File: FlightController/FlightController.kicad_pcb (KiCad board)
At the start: 6 copper layers, 45 x 44 mm, 30 parts, among them J1 FTSH-107-01-L-DV-K-A, J3 M55-7104042R, J5 Conn_01x02_Pin, SW1 SW_TL1015AF160QG, SW2 SW_TL1015AF160QG, U1 STM32L496RGT6TR, U5 BNO086, U9 TCAN332DCNR, Y2 XTAL_ABS07-32.768KHZ-T

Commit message: Updates to FC
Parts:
- removed J1: FTSH-107-01-L-DV-K-A, inspirefly:SAMTEC_FTSH-107-01-L-DV-K-A
- added C8: 100nF, Capacitor_SMD:C_0402_1005Metric_Pad0.74x0.62mm_HandSolder, F.Cu at (154.9, 78.0)
- added C9: 47uF, Capacitor_SMD:C_1206_3216Metric_Pad1.33x1.80mm_HandSolder, F.Cu at (99.9, 54.6)
- added IC1: MX25L25645GM2I-08G-TR, Package_SO:SOIC-8_5.3x5.3mm_P1.27mm, F.Cu at (148.3, 82.5)
- C1, C18, C2, C22, C24, C25, C26, C27, C28, C3, C33, C4, C5, C6, C7: footprint Capacitor_SMD:C_0402_1005Metric -> Capacitor_SMD:C_0402_1005Metric_Pad0.74x0.62mm_HandSolder
- R10, R2, R22, R25, R7: footprint Resistor_SMD:R_0402_1005Metric -> Resistor_SMD:R_0402_1005Metric_Pad0.72x0.64mm_HandSolder
- moved RN1 84.0 mm to (167.8, 65.3)
- moved SW2 70.6 mm to (169.1, 50.9)
- moved SW1 69.1 mm to (170.1, 55.9)
- moved C2 64.8 mm to (154.6, 44.9)
- moved C3 64.8 mm to (154.6, 46.8)
- moved C1 62.3 mm to (153.8, 53.5)
- moved Y2 58.7 mm to (159.2, 46.5)
- moved U9 47.4 mm to (125.5, 83.4)
- moved J5 42.0 mm to (72.8, 45.7)
- moved R2 41.9 mm to (150.8, 55.9)
- moved C4 40.7 mm to (132.3, 67.6)
- moved C5 40.7 mm to (132.3, 69.5)
- moved R7 39.7 mm to (149.4, 52.5)
- moved C22 38.4 mm to (131.7, 72.2)
- moved C33 37.3 mm to (130.0, 80.6)
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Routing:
- net +3.3V: track 0.00 -> 28.6 mm, vias 0 -> 5
- added copper zone on In2.Cu, net +3.3V
- removed copper zone on In3.Cu, net +3.3V
- removed copper zone on In2.Cu, net GND
- removed copper zone on In4.Cu, net GND
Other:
- copper layers 6 -> 4

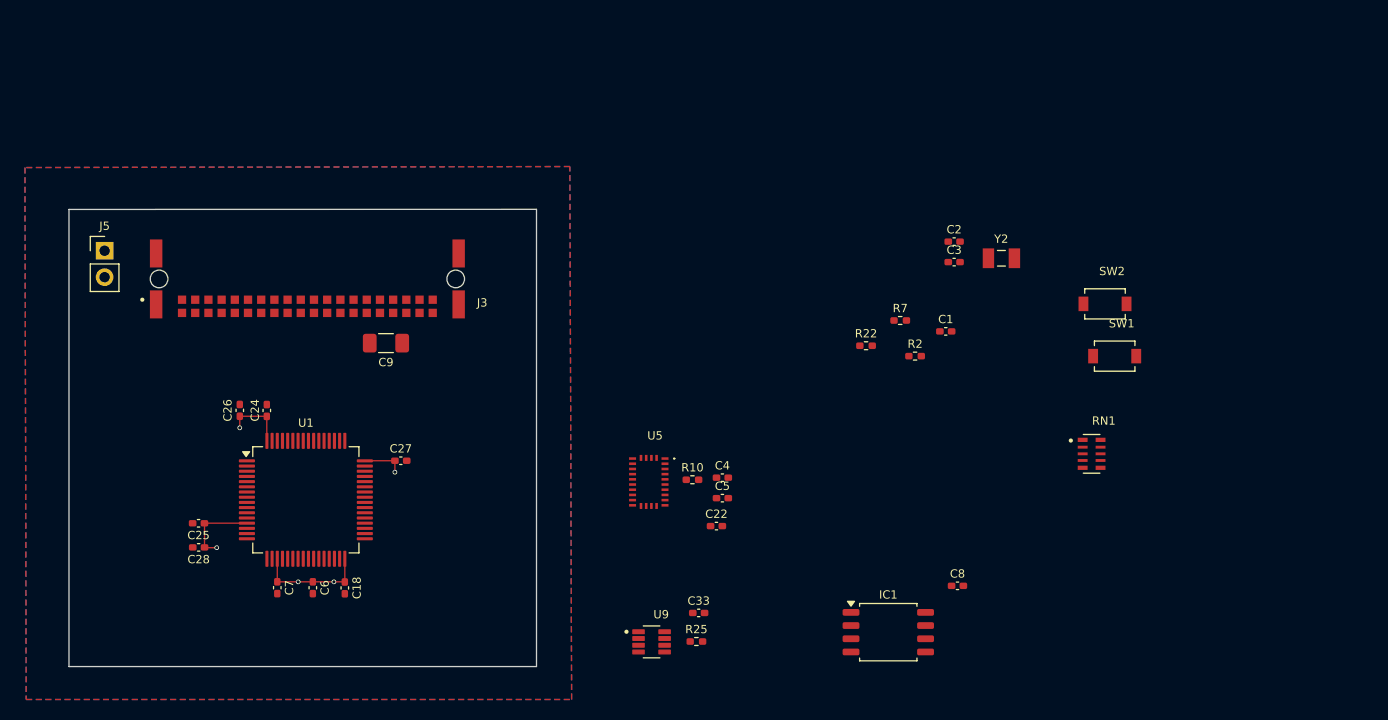
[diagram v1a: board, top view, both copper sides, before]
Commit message: Sorting files/ cleanup
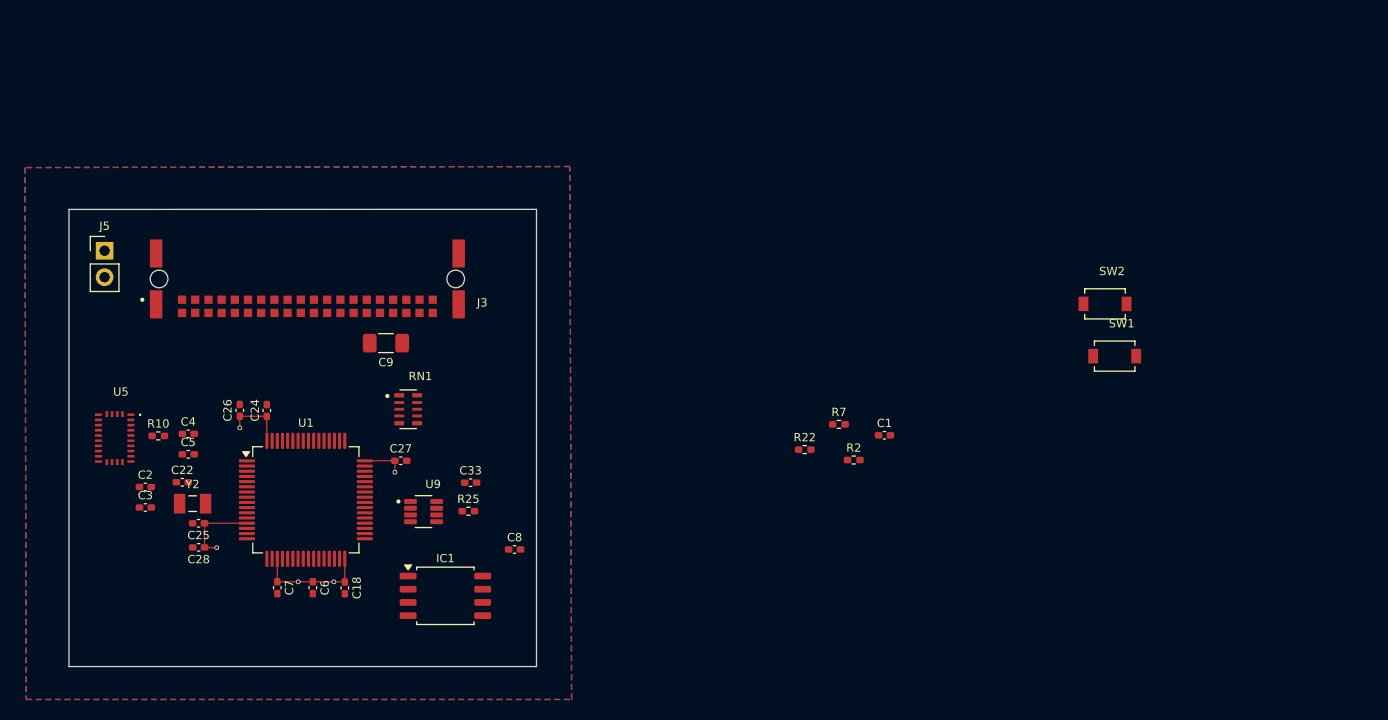
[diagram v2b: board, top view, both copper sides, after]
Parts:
- moved Y2 81.4 mm to (81.3, 70.1)
- moved C2 81.4 mm to (76.8, 68.5)
- moved C3 81.4 mm to (76.8, 70.5)
- moved RN1 65.9 mm to (102.0, 61.0)
- moved C22 51.6 mm to (80.3, 68.0)
- moved C4 51.6 mm to (80.9, 63.4)
- moved C5 51.6 mm to (80.9, 65.3)
- moved R10 51.6 mm to (78.0, 63.6)
- moved U5 51.6 mm to (73.8, 63.8)
- moved IC1 42.8 mm to (105.6, 79.0)
- moved C8 42.8 mm to (112.3, 74.5)
- moved U9 25.3 mm to (103.5, 70.8)
- moved C33 25.3 mm to (108.1, 68.1)
- moved R25 25.3 mm to (107.8, 70.8)
- moved R7 11.6 mm to (143.5, 62.5)
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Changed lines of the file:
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@@
 	(footprint "Capacitor_SMD:C_0402_1005Metric_Pad0.74x0.62mm_HandSolder"
 		(layer "F.Cu")
-		(at 153.7925 53.5)
+		(at 147.8925 63.5)
 		(descr "Capacitor SMD 0402 (1005 Metric), square (rectangular) end terminal, IPC-7351 nominal with elongated pad for handsoldering. (Body size source: IPC-SM-782 page 76, https://www.pcb-3d.com/wordpress/wp-content/uploads/ipc-sm-782a_amendment_1_and_2.pdf), generated with kicad-footprint-generator")
 		(tags "capacitor handsolder")
@@
 	(footprint "Package_SO:SOIC-8_5.3x5.3mm_P1.27mm"
 		(layer "F.Cu")
-		(at 148.26 82.45)
+		(at 105.63 78.9525)
 		(descr "SOIC, 8 Pin (JEITA/EIAJ ED-7311-19 variation 08-001-BBA and Atmel/Microchip, 208 mils width, https://www.jeita.or.jp/japanese/standard/book/ED-7311-19/#target/page_no=21, https://ww1.microchip.com/downloads/en/DeviceDoc/20005045C.pdf#page=23, https://ww1.microchip.com/downloads/en/DeviceDoc/doc2535.pdf#page=162), generated with kicad-footprint-generator ipc_gullwing_generator.py")
 		(tags "SOIC SO P-SOP SOP SOP-8 SO SO-8 8S2 S2AE/F K04-056 CASE-751BE SO8W 8-Pin-SOIC PSA W8-2 W8-4 W8MS-1 FPT-8P-M08")
@@
 	(footprint "Capacitor_SMD:C_0402_1005Metric_Pad0.74x0.62mm_HandSolder"
 		(layer "F.Cu")
-		(at 132.2925 69.55)
+		(at 80.88 65.33)
 		(descr "Capacitor SMD 0402 (1005 Metric), square (rectangular) end terminal, IPC-7351 nominal with elongated pad for handsoldering. (Body size source: IPC-SM-782 page 76, https://www.pcb-3d.com/wordpress/wp-content/uploads/ipc-sm-782a_amendment_1_and_2.pdf), generated with kicad-footprint-generator")
 		(tags "capacitor handsolder")
@@
 	(footprint "inspirefly:BNO086"
 		(layer "F.Cu")
-		(at 125.208 67.99)
+		(at 73.7955 63.77)
 		(descr "BNO086-1")
 		(tags "Undefined or Miscellaneous")
@@
 	(footprint "Resistor_SMD:R_0402_1005Metric_Pad0.72x0.64mm_HandSolder"
 		(layer "F.Cu")
-		(at 129.41 67.78)
+		(at 77.9975 63.56)
 		(descr "Resistor SMD 0402 (1005 Metric), square (rectangular) end terminal, IPC-7351 nominal with elongated pad for handsoldering. (Body size source: IPC-SM-782 page 72, https://www.pcb-3d.com/wordpress/wp-content/uploads/ipc-sm-782a_amendment_1_and_2.pdf), generated with kicad-footprint-generator")
 		(tags "resistor handsolder")
@@
 	(footprint "Resistor_SMD:R_0402_1005Metric_Pad0.72x0.64mm_HandSolder"
 		(layer "F.Cu")
-		(at 146.12 54.88)
+		(at 140.22 64.88)
 		(descr "Resistor SMD 0402 (1005 Metric), square (rectangular) end terminal, IPC-7351 nominal with elongated pad for handsoldering. (Body size source: IPC-SM-782 page 72, https://www.pcb-3d.com/wordpress/wp-content/uploads/ipc-sm-782a_amendment_1_and_2.pdf), generated with kicad-footprint-generator")
 		(tags "resistor handsolder")
@@
 	(footprint "Capacitor_SMD:C_0402_1005Metric_Pad0.74x0.62mm_HandSolder"
 		(layer "F.Cu")
-		(at 154.6 44.86)
+		(at 76.75 68.48)
 		(descr "Capacitor SMD 0402 (1005 Metric), square (rectangular) end terminal, IPC-7351 nominal with elongated pad for handsoldering. (Body size source: IPC-SM-782 page 76, https://www.pcb-3d.com/wordpress/wp-content/uploads/ipc-sm-782a_amendment_1_and_2.pdf), generated with kicad-footprint-generator")
 		(tags "capacitor handsolder")
@@
 	(footprint "inspirefly:XTAL_ABS07-32.768KHZ-T"
 		(layer "F.Cu")
-		(at 159.15 46.46)
+		(at 81.3 70.08)
 		(property "Reference" "Y2"
 			(at -0.018 -1.8564 0)
@@
 	(footprint "Capacitor_SMD:C_0402_1005Metric_Pad0.74x0.62mm_HandSolder"
 		(layer "F.Cu")
-		(at 131.72 72.24)
+		(at 80.3075 68.02)
 		(descr "Capacitor SMD 0402 (1005 Metric), square (rectangular) end terminal, IPC-7351 nominal with elongated pad for handsoldering. (Body size source: IPC-SM-782 page 76, https://www.pcb-3d.com/wordpress/wp-content/uploads/ipc-sm-782a_amendment_1_and_2.pdf), generated with kicad-footprint-generator")
 		(tags "capacitor handsolder")
@@
 	(footprint "Capacitor_SMD:C_0402_1005Metric_Pad0.74x0.62mm_HandSolder"
 		(layer "F.Cu")
-		(at 154.6 46.83)
+		(at 76.75 70.45)
 		(descr "Capacitor SMD 0402 (1005 Metric), square (rectangular) end terminal, IPC-7351 nominal with elongated pad for handsoldering. (Body size source: IPC-SM-782 page 76, https://www.pcb-3d.com/wordpress/wp-content/uploads/ipc-sm-782a_amendment_1_and_2.pdf), generated with kicad-footprint-generator")
 		(tags "capacitor handsolder")
@@
 	(footprint "Resistor_SMD:R_0402_1005Metric_Pad0.72x0.64mm_HandSolder"
 		(layer "F.Cu")
-		(at 149.41 52.45)
+		(at 143.51 62.45)
 		(descr "Resistor SMD 0402 (1005 Metric), square (rectangular) end terminal, IPC-7351 nominal with elongated pad for handsoldering. (Body size source: IPC-SM-782 page 72, https://www.pcb-3d.com/wordpress/wp-content/uploads/ipc-sm-782a_amendment_1_and_2.pdf), generated with kicad-footprint-generator")
 		(tags "resistor handsolder")
@@
 	(footprint "inspirefly:SOT65P280X145-8N"
 		(layer "F.Cu")
-		(at 125.475 83.385)
+		(at 103.525 70.845)
 		(property "Reference" "U9"
 			(at 0.925 -2.635 0)
@@
 	(footprint "Capacitor_SMD:C_0402_1005Metric_Pad0.74x0.62mm_HandSolder"
 		(layer "F.Cu")
-		(at 154.92 77.99)
+		(at 112.29 74.4925)
 		(descr "Capacitor SMD 0402 (1005 Metric), square (rectangular) end terminal, IPC-7351 nominal with elongated pad for handsoldering. (Body size source: IPC-SM-782 page 76, https://www.pcb-3d.com/wordpress/wp-content/uploads/ipc-sm-782a_amendment_1_and_2.pdf), generated with kicad-footprint-generator")
 		(tags "capacitor handsolder")
@@
 	(footprint "Resistor_SMD:R_0402_1005Metric_Pad0.72x0.64mm_HandSolder"
 		(layer "F.Cu")
-		(at 150.84 55.88)
+		(at 144.94 65.88)
 		(descr "Resistor SMD 0402 (1005 Metric), square (rectangular) end terminal, IPC-7351 nominal with elongated pad for handsoldering. (Body size source: IPC-SM-782 page 72, https://www.pcb-3d.com/wordpress/wp-content/uploads/ipc-sm-782a_amendment_1_and_2.pdf), generated with kicad-footprint-generator")
 		(tags "resistor handsolder")
@@
 	(footprint "Resistor_SMD:R_0402_1005Metric_Pad0.72x0.64mm_HandSolder"
 		(layer "F.Cu")
-		(at 129.79 83.35)
+		(at 107.84 70.81)
 		(descr "Resistor SMD 0402 (1005 Metric), square (rectangular) end terminal, IPC-7351 nominal with elongated pad for handsoldering. (Body size source: IPC-SM-782 page 72, https://www.pcb-3d.com/wordpress/wp-content/uploads/ipc-sm-782a_amendment_1_and_2.pdf), generated with kicad-footprint-generator")
 		(tags "resistor handsolder")
@@
 	(footprint "Capacitor_SMD:C_0402_1005Metric_Pad0.74x0.62mm_HandSolder"
 		(layer "F.Cu")
-		(at 132.2925 67.58)
+		(at 80.88 63.36)
 		(descr "Capacitor SMD 0402 (1005 Metric), square (rectangular) end terminal, IPC-7351 nominal with elongated pad for handsoldering. (Body size source: IPC-SM-782 page 76, https://www.pcb-3d.com/wordpress/wp-content/uploads/ipc-sm-782a_amendment_1_and_2.pdf), generated with kicad-footprint-generator")
 		(tags "capacitor handsolder")
@@
 	(footprint "Capacitor_SMD:C_0402_1005Metric_Pad0.74x0.62mm_HandSolder"
 		(layer "F.Cu")
-		(at 130.01 80.6)
+		(at 108.06 68.06)
 		(descr "Capacitor SMD 0402 (1005 Metric), square (rectangular) end terminal, IPC-7351 nominal with elongated pad for handsoldering. (Body size source: IPC-SM-782 page 76, https://www.pcb-3d.com/wordpress/wp-content/uploads/ipc-sm-782a_amendment_1_and_2.pdf), generated with kicad-footprint-generator")
 		(tags "capacitor handsolder")
@@
 	(footprint "inspirefly:RESCAXE64P320X160X70-10N"
 		(layer "F.Cu")
-		(at 167.83 65.285)
+		(at 102.05 60.995)
 		(property "Reference" "RN1"
 			(at 1.175 -3.175 0)

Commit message: Board sizes for FC and routing. slight Backplane changes
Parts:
- removed C25: 10nF, Capacitor_SMD:C_0402_1005Metric_Pad0.74x0.62mm_HandSolder
- added C10: 22pF, Capacitor_SMD:C_0402_1005Metric_Pad0.74x0.62mm_HandSolder, F.Cu at (106.7, 48.1)
- added C11: 22pF, Capacitor_SMD:C_0402_1005Metric_Pad0.74x0.62mm_HandSolder, F.Cu at (106.7, 45.5)
- added H5: MountingHole_Pad, inspirefly:MountingHole_2mm_custom, F.Cu at (75.6, 37.0)
- added H6: MountingHole_Pad, inspirefly:MountingHole_2mm_custom, F.Cu at (108.6, 37.0)
- added Y3: XTAL_ABS07-32.768KHZ-T, inspirefly:XTAL_ABS07-32.768KHZ-T, F.Cu at (109.2, 46.6)
- moved SW2 88.9 mm to (81.3, 36.9)
- moved SW1 82.3 mm to (90.0, 36.9)
- moved R2 69.5 mm to (76.3, 55.0)
- moved C1 69.4 mm to (79.0, 55.0), turned to 180 degrees
- moved R7 63.7 mm to (85.6, 35.9)
- moved R22 60.7 mm to (85.6, 38.3), turned to 180 degrees
- moved J5 43.5 mm to (109.8, 68.7)
- moved IC1 41.7 mm to (99.4, 37.7)
- moved C8 39.9 mm to (105.2, 35.2), turned to 90 degrees
- moved C22 35.1 mm to (105.0, 43.0), turned to 90 degrees
- moved C33 35.0 mm to (85.5, 41.3), turned to 180 degrees
- moved R25 33.2 mm to (92.8, 41.2), turned to 90 degrees
- moved U9 33.0 mm to (89.5, 41.0)
- moved U5 33.0 mm to (102.8, 48.0)
- moved RN1 31.9 mm to (75.8, 42.9)
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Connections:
- J3 pad A17: GND -> SUPER_CAP_CHARGE
- U1 pad 27: IMU_BOOTN -> unconnected-(U1A-PB1-Pad27)
- U1 pad 37: unconnected-(U1A-PC6-Pad37) -> FOOTSWITCH
- U1 pad 38: EXTERNAL_BAT_CUTOFF -> SUPER_CAP_CHARGE
- U1 pad 39: HEATER_ENABLE -> IMU_BOOTN
- U5 pad 26: GND -> Net-(U5-XOUT32/CLKSEL1)
- U5 pad 27: unconnected-(U5-XIN32-Pad27) -> Net-(U5-XIN32)
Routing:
- net I2C2_SDA: track 0.00 -> 65.3 mm, vias 0 -> 4
- net I2C4_SDA: track 0.00 -> 60.8 mm, vias 0 -> 2
- net CAN_H: track 0.00 -> 57.9 mm, vias 0 -> 2
- net ANT_SPI2_MISO: track 0.00 -> 56.6 mm, vias 0 -> 5
- net I2C3_SCL: track 0.00 -> 52.9 mm, vias 0 -> 3
- net I2C2_SCL: track 0.00 -> 52.3 mm, vias 0 -> 4
- net I2C4_SCL: track 0.00 -> 51.5 mm, vias 0 -> 2
- net I2C3_SDA: track 0.00 -> 50.5 mm, vias 0 -> 3
- net IMU_NRST: track 0.00 -> 49.4 mm, vias 0 -> 2
- net NRST: track 0.00 -> 49.3 mm, vias 0 -> 3
- net I2C1_SDA: track 0.00 -> 49.0 mm, vias 0 -> 2
- net I2C1_SCL: track 0.00 -> 48.9 mm, vias 0 -> 2
- net CAN_L: track 0.00 -> 41.8 mm, vias 0 -> 2
- net +3.3V: track 28.6 -> 68.3 mm, vias 5 -> 25
- net ADC1_A1: track 0.00 -> 37.7 mm, vias 0 -> 4
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- added copper zone on F.Cu, net +3.3V
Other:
- board size 45 x 44 mm -> 40 x 40 mm

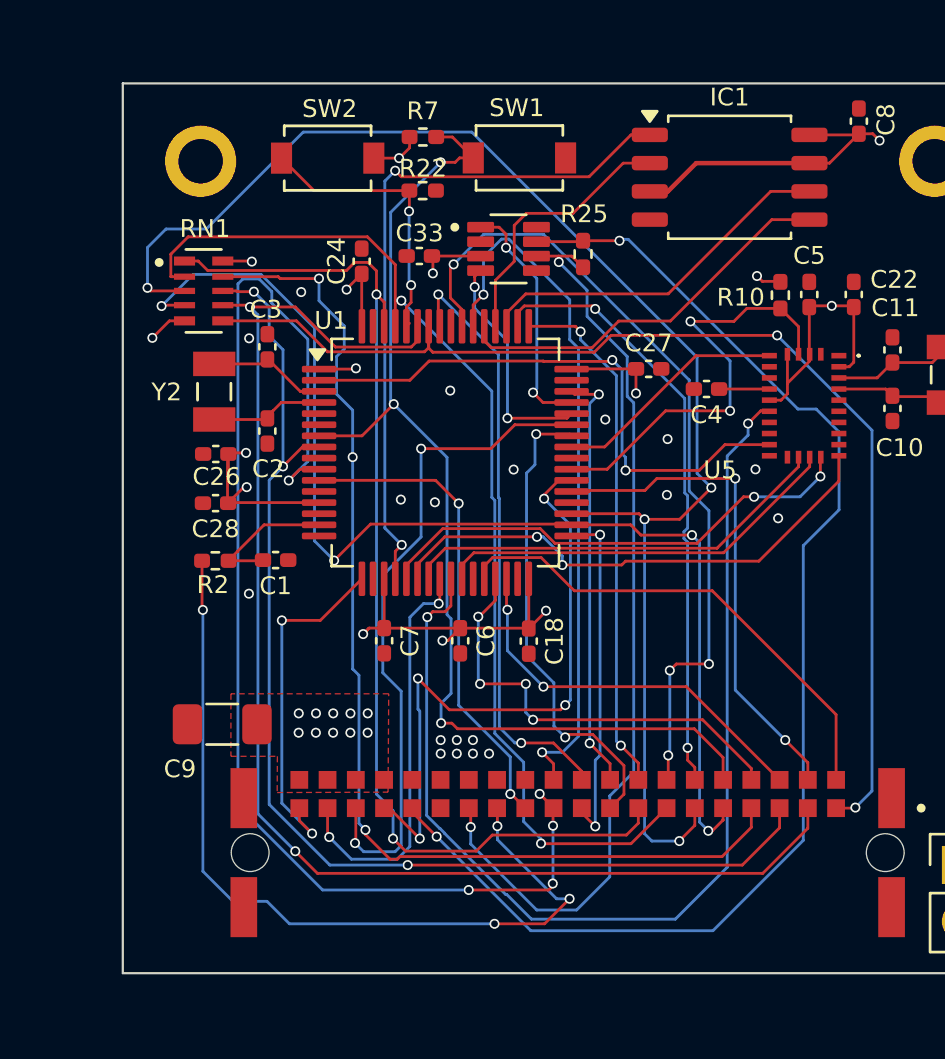
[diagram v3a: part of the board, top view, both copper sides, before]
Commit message: Routing and schematic work on most boards
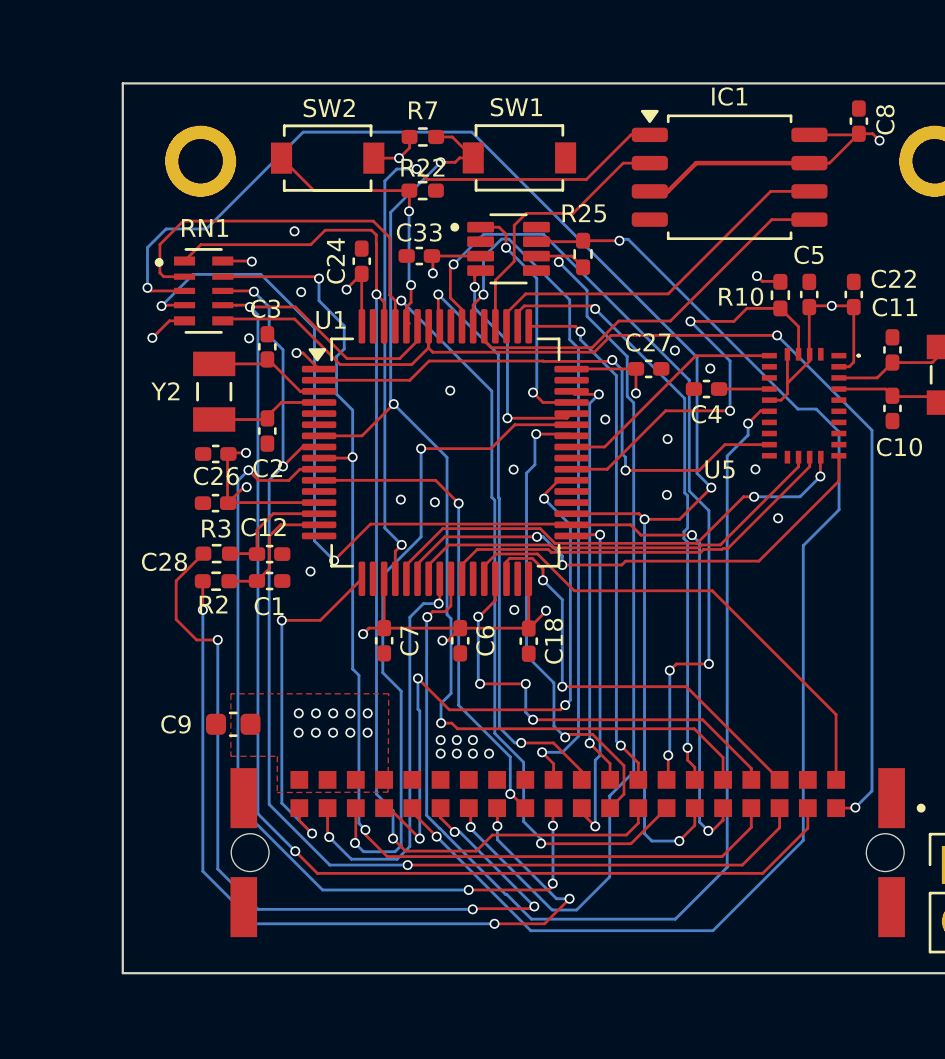
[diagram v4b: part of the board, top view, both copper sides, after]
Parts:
- added C12: 10nF, Capacitor_SMD:C_0402_1005Metric_Pad0.74x0.62mm_HandSolder, F.Cu at (78.7, 54.7)
- added R3: 1k, Resistor_SMD:R_0402_1005Metric_Pad0.72x0.64mm_HandSolder, F.Cu at (76.4, 54.7)
- C1: value 100nF -> 10nF
- C9: value 47uF -> 10uF; footprint Capacitor_SMD:C_1206_3216Metric_Pad1.33x1.80mm_HandSolder -> Capacitor_SMD:C_0603_1608Metric
- moved C1 0.98 mm to (78.7, 55.9)
- moved R2 0.92 mm to (76.3, 55.9)
- moved C9 0.50 mm to (77.1, 62.3)
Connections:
- net SUPER_CAP_CHARGE renamed EN_THERMISTOR_READ
- J3 pad A15: GND -> ADC1_A2
- J3 pad B2: FOOTSWITCH -> unconnected-(J3-PadB2)
- U1 pad 14: unconnected-(U1A-PA0-Pad14) -> Net-(U1A-PA0)
- U1 pad 37: FOOTSWITCH -> unconnected-(U1A-PC6-Pad37)
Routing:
- net ADC1_A2: track 0.00 -> 37.4 mm, vias 0 -> 4
- net FOOTSWITCH: track 22.5 -> 0.00 mm, vias 2 -> 0
- net ANT_SPI2_MISO: track 56.6 -> 38.2 mm, vias 5 -> 4
- net Net-(U1A-PA0): track 0.00 -> 5.40 mm
- net I2C1_SCL: track 48.9 -> 51.2 mm
- net DEBUG_LPUART_TX: track 17.9 -> 19.8 mm
- net I2C1_SDA: track 49.0 -> 50.8 mm
- net +3.3V: track 68.3 -> 66.8 mm
- net I2C3_SDA: track 50.5 -> 51.9 mm
- net ADC1_A1: track 37.7 -> 36.8 mm
- net I2C4_SCL: track 51.5 -> 52.0 mm
- net GND: vias 19 -> 23

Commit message: Finalize board work + BOM work
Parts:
- added G***: LOGO, inspireFly:longInspireFly_12mmX4mm, F.Cu at (99.9, 59.2)
- C6: footprint Capacitor_SMD:C_0402_1005Metric_Pad0.74x0.62mm_HandSolder -> Capacitor_SMD:C_0603_1608Metric
- moved C6 0.11 mm to (87.3, 58.7)
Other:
- board text added: "Flight Controller PQ V0.1"
